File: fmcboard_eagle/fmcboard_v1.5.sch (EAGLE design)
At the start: 176 parts, among them IC1 OPA699ID, IC10 LTC6229IMS8E#TRPBF, IC11 7805TV, IC12 SN74AUC2G66DCTR, IC13 SN74AUC2G66DCTR, IC14 SN74AUC2G66DCTR, IC15 SN74AUC2G66DCTR, IC16 DAC7578SPWR, IC17 SN74AUC2G66DCTR, IC18 SN74AUC2G66DCTR, IC19 SN74AUC2G66DCTR, IC2 DAC7578SPWR, IC20 SN74AUC2G66DCTR, IC21 74AUP2GU04GW,125, IC22 74AUP2GU04GW,125, IC23 74AUP2GU04GW,125, IC24 74AUP2GU04GW,125, IC25 LM358, IC3 LTC6229IMS8E#TRPBF, IC4 LTC6229IMS8E#TRPBF, IC6 OPA699ID, IC7 OPA699ID, IC8 LTC6229IMS8E#TRPBF, IC9 LTC6229IMS8E#TRPBF, J1 8pin, J10 8pin, J12 4p-2.54, J2 ASP-134604-01, J3 4p-2.54, J4 4p-2.54, J5 8pin, J6 4p-2.54, J7 4p-2.54, J8 4p-2.54, J9 8pin, U1 TXS0108EPWR, U2 STMICROELECTRONICS_L7905ACVST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

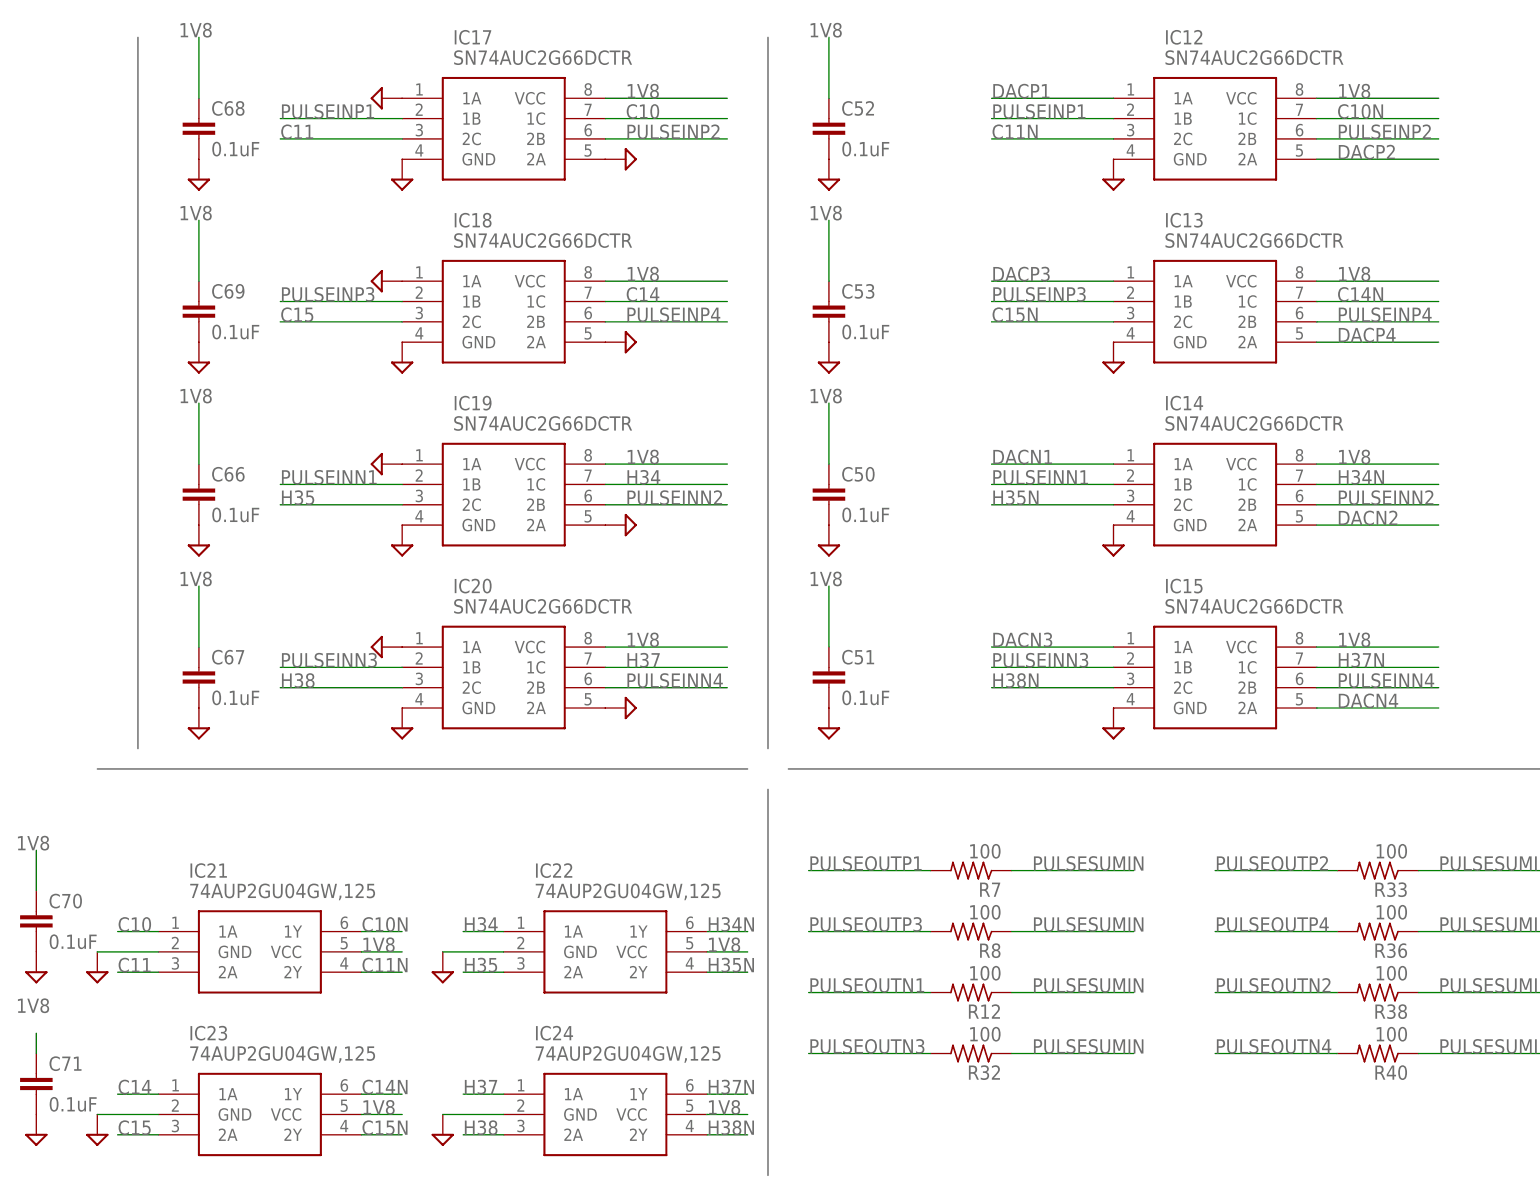
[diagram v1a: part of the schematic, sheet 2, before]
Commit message: make gnd switches on N inverters
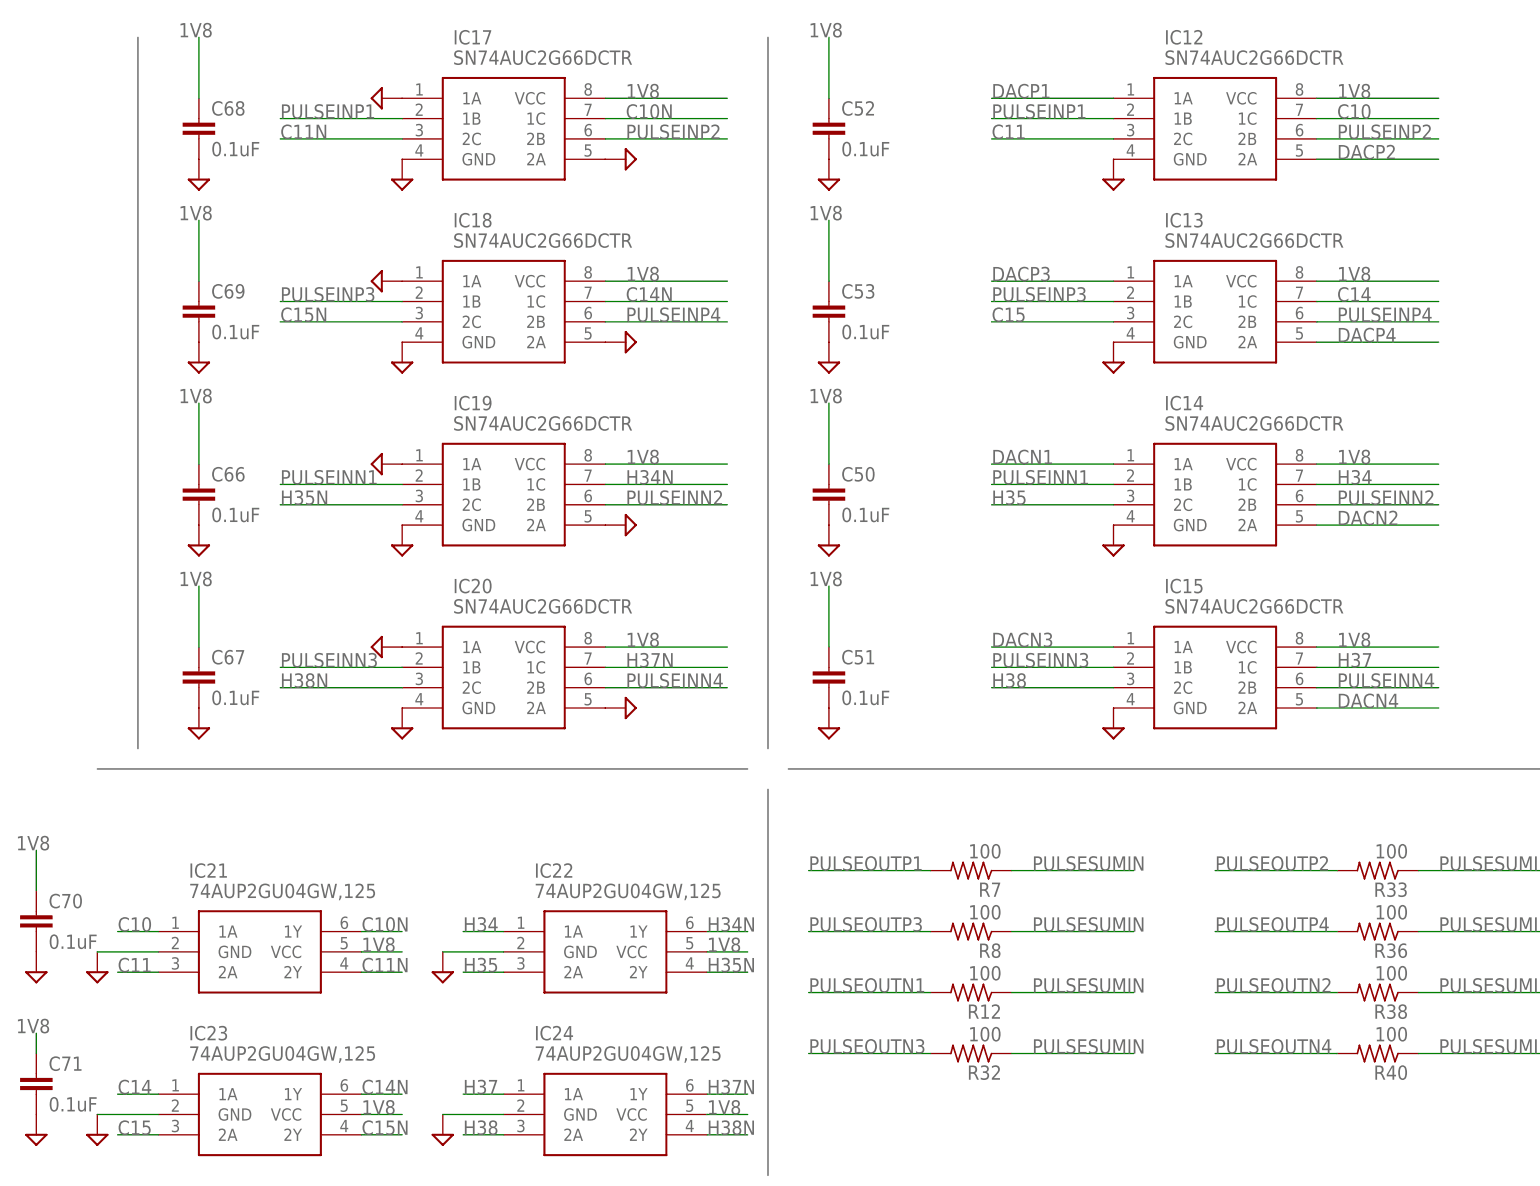
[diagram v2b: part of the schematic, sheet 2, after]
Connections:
- net C10: now also IC12.1C; no longer IC17.1C
- net C10N: now also IC17.1C; no longer IC12.1C
- net C11: now also IC12.2C; no longer IC17.2C
- net C11N: now also IC17.2C; no longer IC12.2C
- net C14: now also IC13.1C; no longer IC18.1C
- net C14N: now also IC18.1C; no longer IC13.1C
- net C15: now also IC13.2C; no longer IC18.2C
- net C15N: now also IC18.2C; no longer IC13.2C
- net H34: now also IC14.1C; no longer IC19.1C
- net H34N: now also IC19.1C; no longer IC14.1C
- net H35: now also IC14.2C; no longer IC19.2C
- net H35N: now also IC19.2C; no longer IC14.2C
- net H37: now also IC15.1C; no longer IC20.1C
- net H37N: now also IC20.1C; no longer IC15.1C
- net H38: now also IC15.2C; no longer IC20.2C
- net H38N: now also IC20.2C; no longer IC15.2C
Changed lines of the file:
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@@
 <net name="H38" class="0">
-<segment>
-<wire x1="-48.26" y1="38.1" x2="-33.02" y2="38.1" width="0.1524" layer="91"/>
-<label x="-48.26" y="38.1" size="1.778" layer="95"/>
-<pinref part="IC20" gate="G$1" pin="2C"/>
-</segment>
 <segment>
 <pinref part="IC24" gate="G$1" pin="2A"/>
@@
 <label x="-25.4" y="-17.78" size="1.778" layer="95"/>
 </segment>
+<segment>
+<wire x1="40.64" y1="38.1" x2="55.88" y2="38.1" width="0.1524" layer="91"/>
+<label x="40.64" y="38.1" size="1.778" layer="95"/>
+<pinref part="IC15" gate="G$1" pin="2C"/>
+</segment>
 </net>
 <net name="H37" class="0">
-<segment>
-<wire x1="-7.62" y1="40.64" x2="7.62" y2="40.64" width="0.1524" layer="91"/>
-<label x="-5.08" y="40.64" size="1.778" layer="95"/>
-<pinref part="IC20" gate="G$1" pin="1C"/>
-</segment>
 <segment>
 <pinref part="IC24" gate="G$1" pin="1A"/>
@@
 <label x="-25.4" y="-12.7" size="1.778" layer="95"/>
 </segment>
+<segment>
+<wire x1="81.28" y1="40.64" x2="96.52" y2="40.64" width="0.1524" layer="91"/>
+<label x="83.82" y="40.64" size="1.778" layer="95"/>
+<pinref part="IC15" gate="G$1" pin="1C"/>
+</segment>
 </net>
 <net name="H35" class="0">
-<segment>
-<wire x1="-48.26" y1="60.96" x2="-33.02" y2="60.96" width="0.1524" layer="91"/>
-<label x="-48.26" y="60.96" size="1.778" layer="95"/>
-<pinref part="IC19" gate="G$1" pin="2C"/>
-</segment>
 <segment>
 <pinref part="IC22" gate="G$1" pin="2A"/>
@@
 <label x="-25.4" y="2.54" size="1.778" layer="95"/>
 </segment>
+<segment>
+<wire x1="40.64" y1="60.96" x2="55.88" y2="60.96" width="0.1524" layer="91"/>
+<label x="40.64" y="60.96" size="1.778" layer="95"/>
+<pinref part="IC14" gate="G$1" pin="2C"/>
+</segment>
 </net>
 <net name="H34" class="0">
-<segment>
-<wire x1="-7.62" y1="63.5" x2="7.62" y2="63.5" width="0.1524" layer="91"/>
-<label x="-5.08" y="63.5" size="1.778" layer="95"/>
-<pinref part="IC19" gate="G$1" pin="1C"/>
-</segment>
 <segment>
 <pinref part="IC22" gate="G$1" pin="1A"/>
 <wire x1="-20.32" y1="7.62" x2="-25.4" y2="7.62" width="0.1524" layer="91"/>
 <label x="-25.4" y="7.62" size="1.778" layer="95"/>
+</segment>
+<segment>
+<wire x1="81.28" y1="63.5" x2="96.52" y2="63.5" width="0.1524" layer="91"/>
+<label x="83.82" y="63.5" size="1.778" layer="95"/>
+<pinref part="IC14" gate="G$1" pin="1C"/>
 </segment>
 </net>
@@
 <net name="C10" class="0">
 <segment>
-<wire x1="-7.62" y1="109.22" x2="7.62" y2="109.22" width="0.1524" layer="91"/>
-<label x="-5.08" y="109.22" size="1.778" layer="95"/>
-<pinref part="IC17" gate="G$1" pin="1C"/>
-</segment>
-<segment>
 <pinref part="IC21" gate="G$1" pin="1A"/>
 <wire x1="-63.5" y1="7.62" x2="-68.58" y2="7.62" width="0.1524" layer="91"/>
 <label x="-68.58" y="7.62" size="1.778" layer="95"/>
 </segment>
+<segment>
+<wire x1="81.28" y1="109.22" x2="96.52" y2="109.22" width="0.1524" layer="91"/>
+<label x="83.82" y="109.22" size="1.778" layer="95"/>
+<pinref part="IC12" gate="G$1" pin="1C"/>
+</segment>
 </net>
 <net name="C11" class="0">
-<segment>
-<wire x1="-48.26" y1="106.68" x2="-33.02" y2="106.68" width="0.1524" layer="91"/>
-<label x="-48.26" y="106.68" size="1.778" layer="95"/>
-<pinref part="IC17" gate="G$1" pin="2C"/>
-</segment>
 <segment>
 <pinref part="IC21" gate="G$1" pin="2A"/>
@@
 <label x="-68.58" y="2.54" size="1.778" layer="95"/>
 </segment>
+<segment>
+<wire x1="40.64" y1="106.68" x2="55.88" y2="106.68" width="0.1524" layer="91"/>
+<label x="40.64" y="106.68" size="1.778" layer="95"/>
+<pinref part="IC12" gate="G$1" pin="2C"/>
+</segment>
 </net>
 <net name="C14" class="0">
-<segment>
-<wire x1="-7.62" y1="86.36" x2="7.62" y2="86.36" width="0.1524" layer="91"/>
-<label x="-5.08" y="86.36" size="1.778" layer="95"/>
-<pinref part="IC18" gate="G$1" pin="1C"/>
-</segment>
 <segment>
 <pinref part="IC23" gate="G$1" pin="1A"/>
@@
 <label x="-68.58" y="-12.7" size="1.778" layer="95"/>
 </segment>
+<segment>
+<wire x1="81.28" y1="86.36" x2="96.52" y2="86.36" width="0.1524" layer="91"/>
+<label x="83.82" y="86.36" size="1.778" layer="95"/>
+<pinref part="IC13" gate="G$1" pin="1C"/>
+</segment>
 </net>
 <net name="C15" class="0">
-<segment>
-<wire x1="-48.26" y1="83.82" x2="-33.02" y2="83.82" width="0.1524" layer="91"/>
-<label x="-48.26" y="83.82" size="1.778" layer="95"/>
-<pinref part="IC18" gate="G$1" pin="2C"/>
-</segment>
 <segment>
 <pinref part="IC23" gate="G$1" pin="2A"/>
 <wire x1="-63.5" y1="-17.78" x2="-68.58" y2="-17.78" width="0.1524" layer="91"/>
 <label x="-68.58" y="-17.78" size="1.778" layer="95"/>
+</segment>
+<segment>
+<wire x1="40.64" y1="83.82" x2="55.88" y2="83.82" width="0.1524" layer="91"/>
+<label x="40.64" y="83.82" size="1.778" layer="95"/>
+<pinref part="IC13" gate="G$1" pin="2C"/>
 </segment>
 </net>
@@
 <pinref part="C71" gate="G$1" pin="1"/>
 <wire x1="-78.74" y1="-7.62" x2="-78.74" y2="-5.08" width="0.1524" layer="91"/>
-<label x="-81.28" y="-2.54" size="1.778" layer="95"/>
+<label x="-81.28" y="-5.08" size="1.778" layer="95"/>
 </segment>
 </net>
@@
 <net name="C11N" class="0">
 <segment>
-<wire x1="40.64" y1="106.68" x2="55.88" y2="106.68" width="0.1524" layer="91"/>
-<label x="40.64" y="106.68" size="1.778" layer="95"/>
-<pinref part="IC12" gate="G$1" pin="2C"/>
-</segment>
-<segment>
 <pinref part="IC21" gate="G$1" pin="2Y"/>
 <wire x1="-38.1" y1="2.54" x2="-33.02" y2="2.54" width="0.1524" layer="91"/>
 <label x="-38.1" y="2.54" size="1.778" layer="95"/>
 </segment>
+<segment>
+<wire x1="-48.26" y1="106.68" x2="-33.02" y2="106.68" width="0.1524" layer="91"/>
+<label x="-48.26" y="106.68" size="1.778" layer="95"/>
+<pinref part="IC17" gate="G$1" pin="2C"/>
+</segment>
 </net>
 <net name="C10N" class="0">
-<segment>
-<wire x1="81.28" y1="109.22" x2="96.52" y2="109.22" width="0.1524" layer="91"/>
-<label x="83.82" y="109.22" size="1.778" layer="95"/>
-<pinref part="IC12" gate="G$1" pin="1C"/>
-</segment>
 <segment>
 <pinref part="IC21" gate="G$1" pin="1Y"/>
@@
 <label x="-38.1" y="7.62" size="1.778" layer="95"/>
 </segment>
+<segment>
+<wire x1="-7.62" y1="109.22" x2="7.62" y2="109.22" width="0.1524" layer="91"/>
+<label x="-5.08" y="109.22" size="1.778" layer="95"/>
+<pinref part="IC17" gate="G$1" pin="1C"/>
+</segment>
 </net>
 <net name="C14N" class="0">
-<segment>
-<wire x1="81.28" y1="86.36" x2="96.52" y2="86.36" width="0.1524" layer="91"/>
-<label x="83.82" y="86.36" size="1.778" layer="95"/>
-<pinref part="IC13" gate="G$1" pin="1C"/>
-</segment>
 <segment>
 <pinref part="IC23" gate="G$1" pin="1Y"/>
@@
 <label x="-38.1" y="-12.7" size="1.778" layer="95"/>
 </segment>
+<segment>
+<wire x1="-7.62" y1="86.36" x2="7.62" y2="86.36" width="0.1524" layer="91"/>
+<label x="-5.08" y="86.36" size="1.778" layer="95"/>
+<pinref part="IC18" gate="G$1" pin="1C"/>
+</segment>
 </net>
 <net name="C15N" class="0">
-<segment>
-<wire x1="40.64" y1="83.82" x2="55.88" y2="83.82" width="0.1524" layer="91"/>
-<label x="40.64" y="83.82" size="1.778" layer="95"/>
-<pinref part="IC13" gate="G$1" pin="2C"/>
-</segment>
 <segment>
 <pinref part="IC23" gate="G$1" pin="2Y"/>
@@
 <label x="-38.1" y="-17.78" size="1.778" layer="95"/>
 </segment>
+<segment>
+<wire x1="-48.26" y1="83.82" x2="-33.02" y2="83.82" width="0.1524" layer="91"/>
+<label x="-48.26" y="83.82" size="1.778" layer="95"/>
+<pinref part="IC18" gate="G$1" pin="2C"/>
+</segment>
 </net>
 <net name="H35N" class="0">
-<segment>
-<wire x1="40.64" y1="60.96" x2="55.88" y2="60.96" width="0.1524" layer="91"/>
-<label x="40.64" y="60.96" size="1.778" layer="95"/>
-<pinref part="IC14" gate="G$1" pin="2C"/>
-</segment>
 <segment>
 <pinref part="IC22" gate="G$1" pin="2Y"/>
@@
 <label x="5.08" y="2.54" size="1.778" layer="95"/>
 </segment>
+<segment>
+<wire x1="-48.26" y1="60.96" x2="-33.02" y2="60.96" width="0.1524" layer="91"/>
+<label x="-48.26" y="60.96" size="1.778" layer="95"/>
+<pinref part="IC19" gate="G$1" pin="2C"/>
+</segment>
 </net>
 <net name="H34N" class="0">
-<segment>
-<wire x1="81.28" y1="63.5" x2="96.52" y2="63.5" width="0.1524" layer="91"/>
-<label x="83.82" y="63.5" size="1.778" layer="95"/>
-<pinref part="IC14" gate="G$1" pin="1C"/>
-</segment>
 <segment>
 <pinref part="IC22" gate="G$1" pin="1Y"/>
@@
 <label x="5.08" y="7.62" size="1.778" layer="95"/>
 </segment>
+<segment>
+<wire x1="-7.62" y1="63.5" x2="7.62" y2="63.5" width="0.1524" layer="91"/>
+<label x="-5.08" y="63.5" size="1.778" layer="95"/>
+<pinref part="IC19" gate="G$1" pin="1C"/>
+</segment>
 </net>
 <net name="H37N" class="0">
-<segment>
-<wire x1="81.28" y1="40.64" x2="96.52" y2="40.64" width="0.1524" layer="91"/>
-<label x="83.82" y="40.64" size="1.778" layer="95"/>
-<pinref part="IC15" gate="G$1" pin="1C"/>
-</segment>
 <segment>
 <pinref part="IC24" gate="G$1" pin="1Y"/>
@@
 <label x="5.08" y="-12.7" size="1.778" layer="95"/>
 </segment>
+<segment>
+<wire x1="-7.62" y1="40.64" x2="7.62" y2="40.64" width="0.1524" layer="91"/>
+<label x="-5.08" y="40.64" size="1.778" layer="95"/>
+<pinref part="IC20" gate="G$1" pin="1C"/>
+</segment>
 </net>
 <net name="H38N" class="0">
-<segment>
-<wire x1="40.64" y1="38.1" x2="55.88" y2="38.1" width="0.1524" layer="91"/>
-<label x="40.64" y="38.1" size="1.778" layer="95"/>
-<pinref part="IC15" gate="G$1" pin="2C"/>
-</segment>
 <segment>
 <pinref part="IC24" gate="G$1" pin="2Y"/>
@@
 <label x="5.08" y="-17.78" size="1.778" layer="95"/>
 </segment>
-</net>
+<segment>
+<wire x1="-48.26" y1="38.1" x2="-33.02" y2="38.1" width="0.1524" layer="91"/>
+<label x="-48.26" y="38.1" size="1.778" layer="95"/>
+<pinref part="IC20" gate="G$1" pin="2C"/>
+</segment>
+</net>
